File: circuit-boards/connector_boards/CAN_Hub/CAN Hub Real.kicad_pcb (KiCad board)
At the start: 2 copper layers, 30.2 x 55.8 mm, 10 parts, among them J1 Conn_01x02_Pin, J2 Conn_01x02_Pin, J3 Conn_01x02_Pin, J4 Conn_01x02_Pin, J5 Conn_01x02_Pin, J6 Conn_01x02_Pin

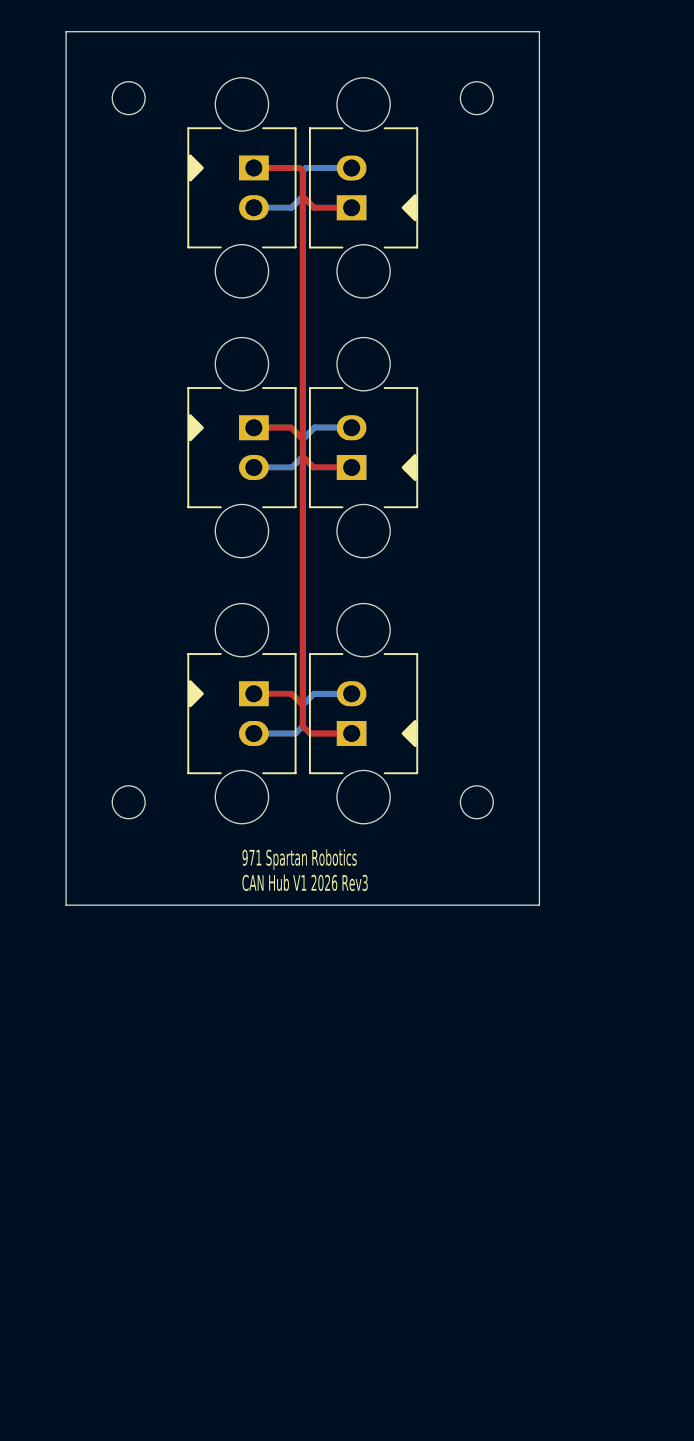
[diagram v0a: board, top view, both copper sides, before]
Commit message: more compact layout, and better routing
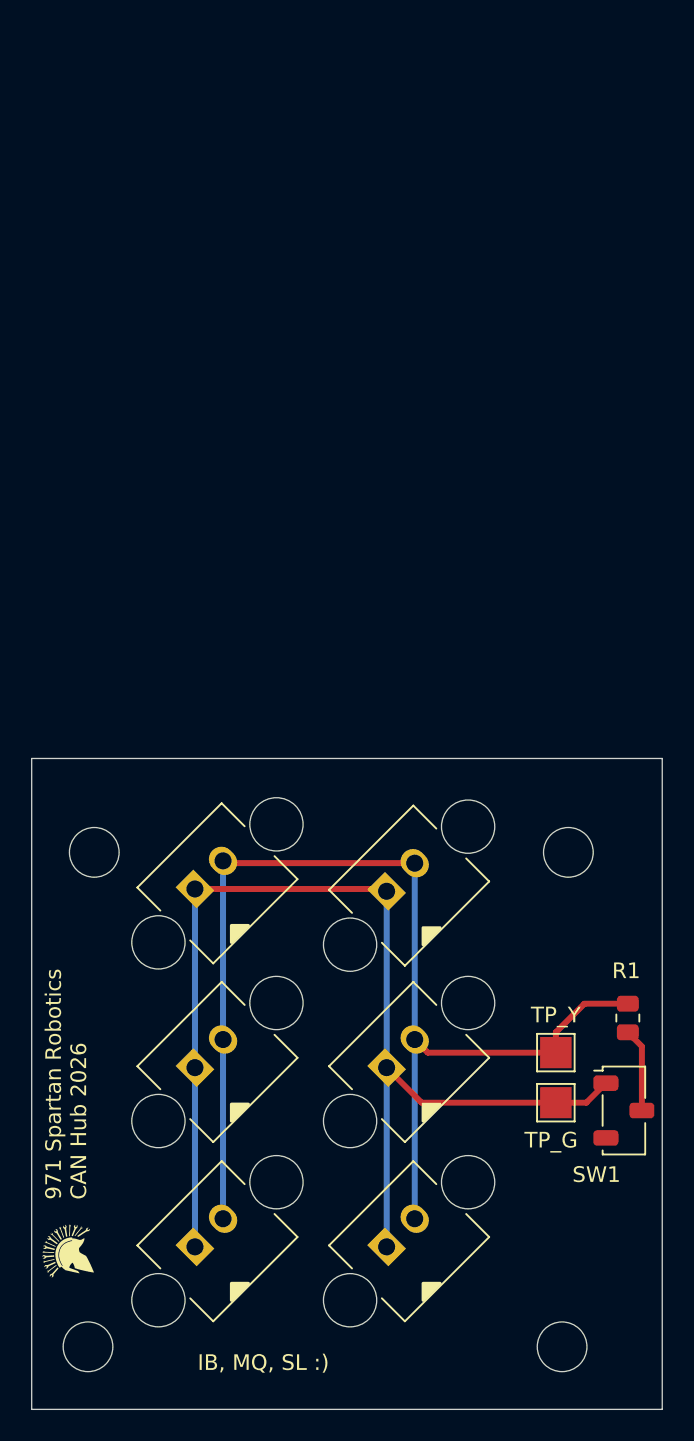
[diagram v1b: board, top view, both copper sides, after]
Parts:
- added G***: spartan_logo, drawings_libary:spartan_logo, F.Cu at (89.6, 102.2)
- added R1: R1, Resistor_SMD:R_0805_2012Metric, F.Cu at (125.4, 87.3)
- added SW1: Termination_1, Button_Switch_SMD:Nidec_Copal_CAS-120A, F.Cu at (125.2, 93.2)
- added TP1: TP_G, TestPoint:TestPoint_Pad_2.0x2.0mm, F.Cu at (120.8, 92.7)
- added TP2: TP_Y, TestPoint:TestPoint_Pad_2.0x2.0mm, F.Cu at (120.8, 89.5)
- H1: footprint MountingHole:MountingHole_2.1mm -> MountingHole:MountingHole_3.175
- H2: renamed from H4; footprint MountingHole:MountingHole_2.1mm -> MountingHole:MountingHole_3.175
- H3: renamed from H2; footprint MountingHole:MountingHole_2.1mm -> MountingHole:MountingHole_3.175
- H4: renamed from H3; footprint MountingHole:MountingHole_2.1mm -> MountingHole:MountingHole_3.175
- moved H3 48.6 mm to (121.6, 76.7)
- moved H1 48.3 mm to (91.3, 76.7)
- moved J1 46.2 mm to (97.7, 79.0), turned to 45 degrees
- moved J4 43.7 mm to (110.0, 79.2), turned to 45 degrees
- moved J2 41.1 mm to (97.7, 90.5), turned to 45 degrees
- moved J5 38.4 mm to (110.0, 90.5), turned to 45 degrees
- moved J3 35.5 mm to (97.7, 101.9), turned to 45 degrees
- moved H4 35.2 mm to (121.2, 108.3)
- moved H2 34.9 mm to (90.9, 108.3)
- moved J6 32.9 mm to (110.0, 101.9), turned to 45 degrees
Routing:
- net /CAN_L: track 55.6 -> 78.9 mm
- net /CAN_H: track 55.6 -> 74.7 mm
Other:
- board size 30.2 x 55.8 mm -> 40.3 x 41.6 mm
- board text added: "971 Spartan Robotics CAN Hub 2026"
- board text added: "IB, MQ, SL :)"
- board text removed: "971 Spartan Robotics CAN Hub V1 2026 Rev3"
